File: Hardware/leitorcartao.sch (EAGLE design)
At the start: 157 parts, among them IC1 TL084, IC2 TL084, Q1 DMN3404, Q4 BC847ALT1SMD, Q5 BC847ALT1SMD, Q6 BC847ALT1SMD, Q7 BC847ALT1SMD, Q8 MMBT4403, Q9 MMBT4401, U1 SAMD20E14A-AUT, U3 TLV1117-50CDCYR, U4 MFRC52202HN1, U5 LP2985-33DBVR, X1 ANTENA 125kHz, X2 MIFARE ANTENA

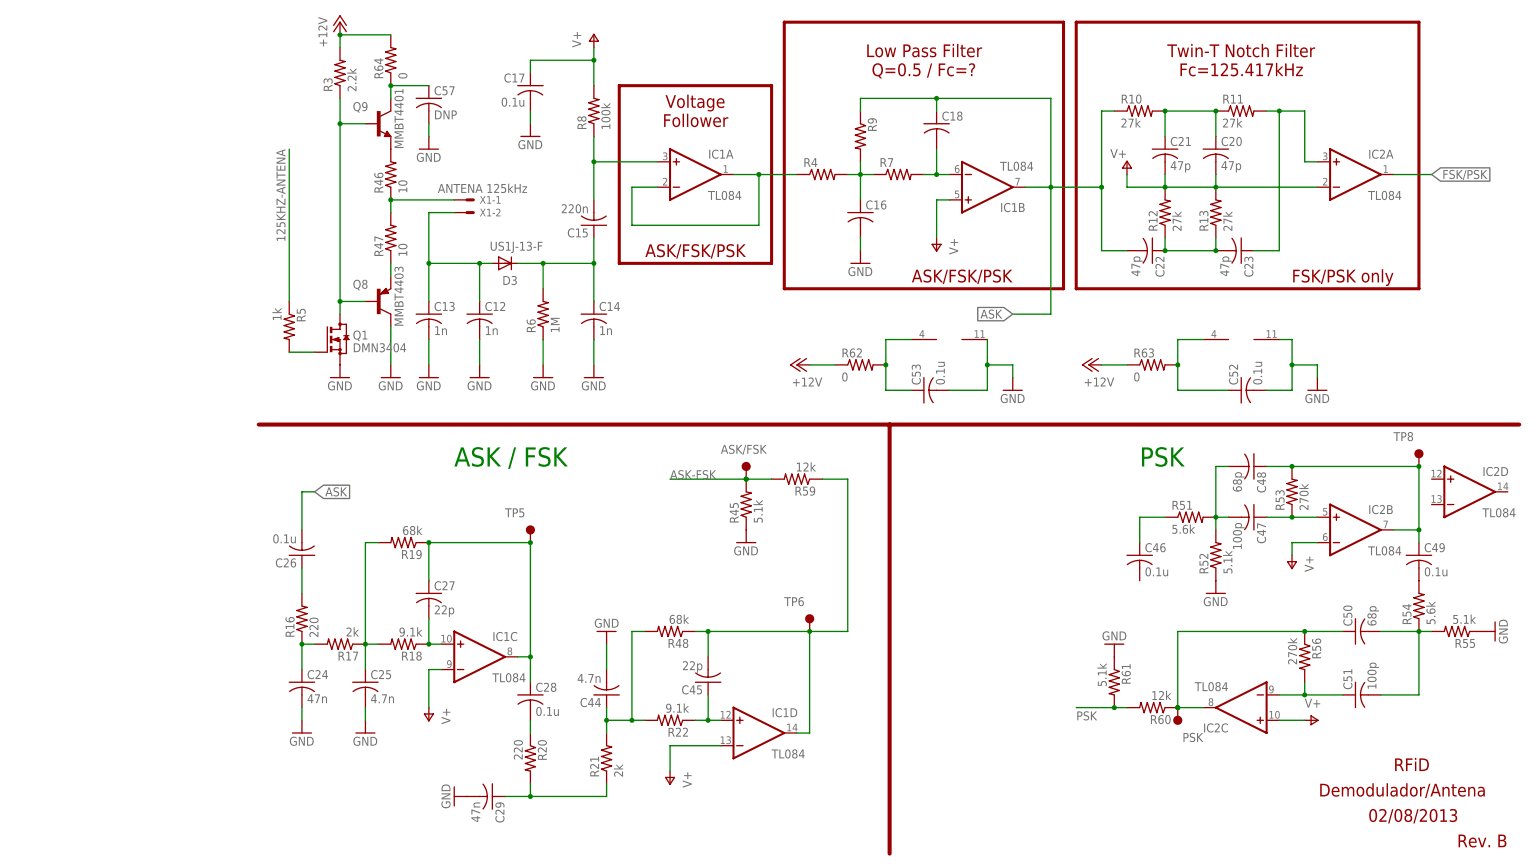
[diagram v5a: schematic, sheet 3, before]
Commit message: Novas alterações do esquema do RFID. ASK com valores já calculados.
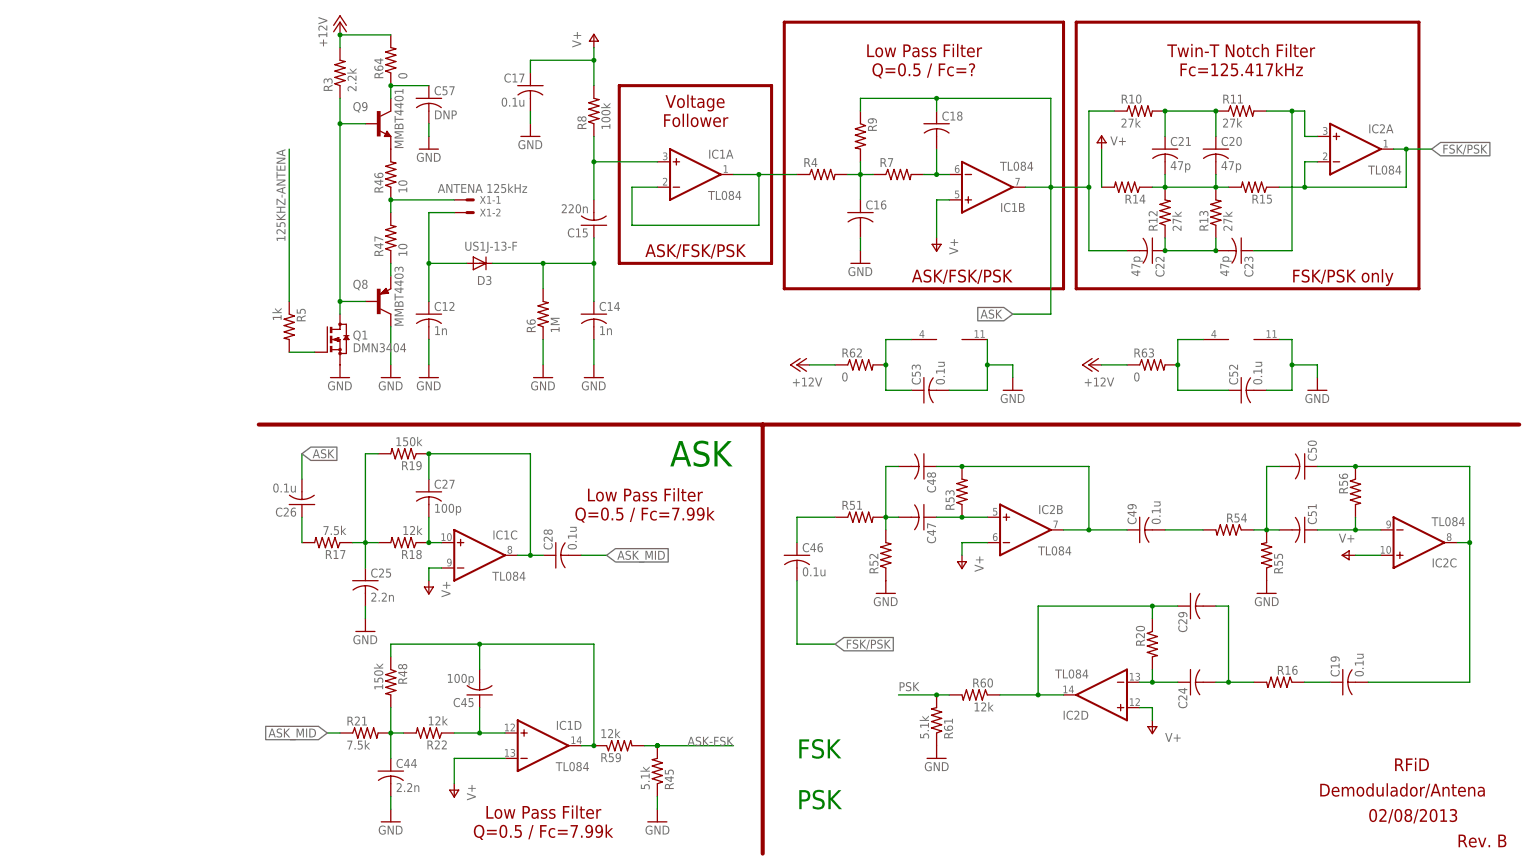
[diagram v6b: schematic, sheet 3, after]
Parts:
- removed ASK/FSK, PSK, TP5, TP6, TP8: TESTPOINT, RFiD:TESTPOINT
- removed C13: 1n, RFiD:C-USC1206
- added C19: 0.1u, RFiD:C-USC0402
- added R14, R15: (no value), RFiD:R-US_R0402
- C24, C29: value 47n -> (none)
- C25, C44: value 4.7n -> 2.2n
- C27, C45: value 22p -> 100p
- C47, C51: value 100p -> (none)
- C48, C50: value 68p -> (none)
- R16, R20: value 220 -> (none)
- R17, R21: value 2k -> 7.5k
- R18, R22: value 9.1k -> 12k
- R19, R48: value 68k -> 150k
- R51, R54: value 5.6k -> (none)
- R52, R55: value 5.1k -> (none)
- R53, R56: value 270k -> (none)
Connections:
- removed net N$22 (its old number): C26.1, R16.2
- removed net N$28: C27.1, C28.1, IC1C.OUT, R19.1, TP5.1
- new net ASK_MID: C28.2, R21.1
- new net N$17: C20.2, C21.2, R12.2, R13.2, R14.1, R15.2
- new net N$21: C26.1, R17.2
- new net N$26: C24.1, IC2D.-IN, R20.2
- new net N$56: C27.1, C28.1, IC1C.OUT, R19.1
- net ASK-FSK: no longer ASK/FSK.1
- net FSK/PSK: now also C46.2, IC2A.-IN, R15.1
- net GND: no longer C13.2, C24.2, C29.2
- net N$24: now also C29.1, IC2D.OUT, R20.1, R60.1; no longer C24.1, R16.1, R17.2
- net N$29: now also C24.2, C29.2, R16.2; no longer C28.2, R20.1
- net N$30: now also C19.1, R16.1; no longer C29.1, R20.2, R21.1
- net N$40: now also C19.2; no longer PSK.1, R60.1
- net N$71: no longer TP8.1
- net N$9: no longer C13.1
- net N$90: no longer TP6.1
- net V+: now also IC2D.+IN, R14.2; no longer C20.2, C21.2, IC2A.-IN, R12.2, R13.2
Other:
- note added: "ASK"
- note added: "FSK"
- note added: "Low Pass Filter Q=0.5 / Fc=7.99k"
- note removed: "ASK / FSK"
- moved on the sheet: C12, C24, C25, C26, C27, C28, C29, C44, C45, C46, C47, C48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

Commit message: Finalização do esquema do RFID, falta valores de PSK e FSK.
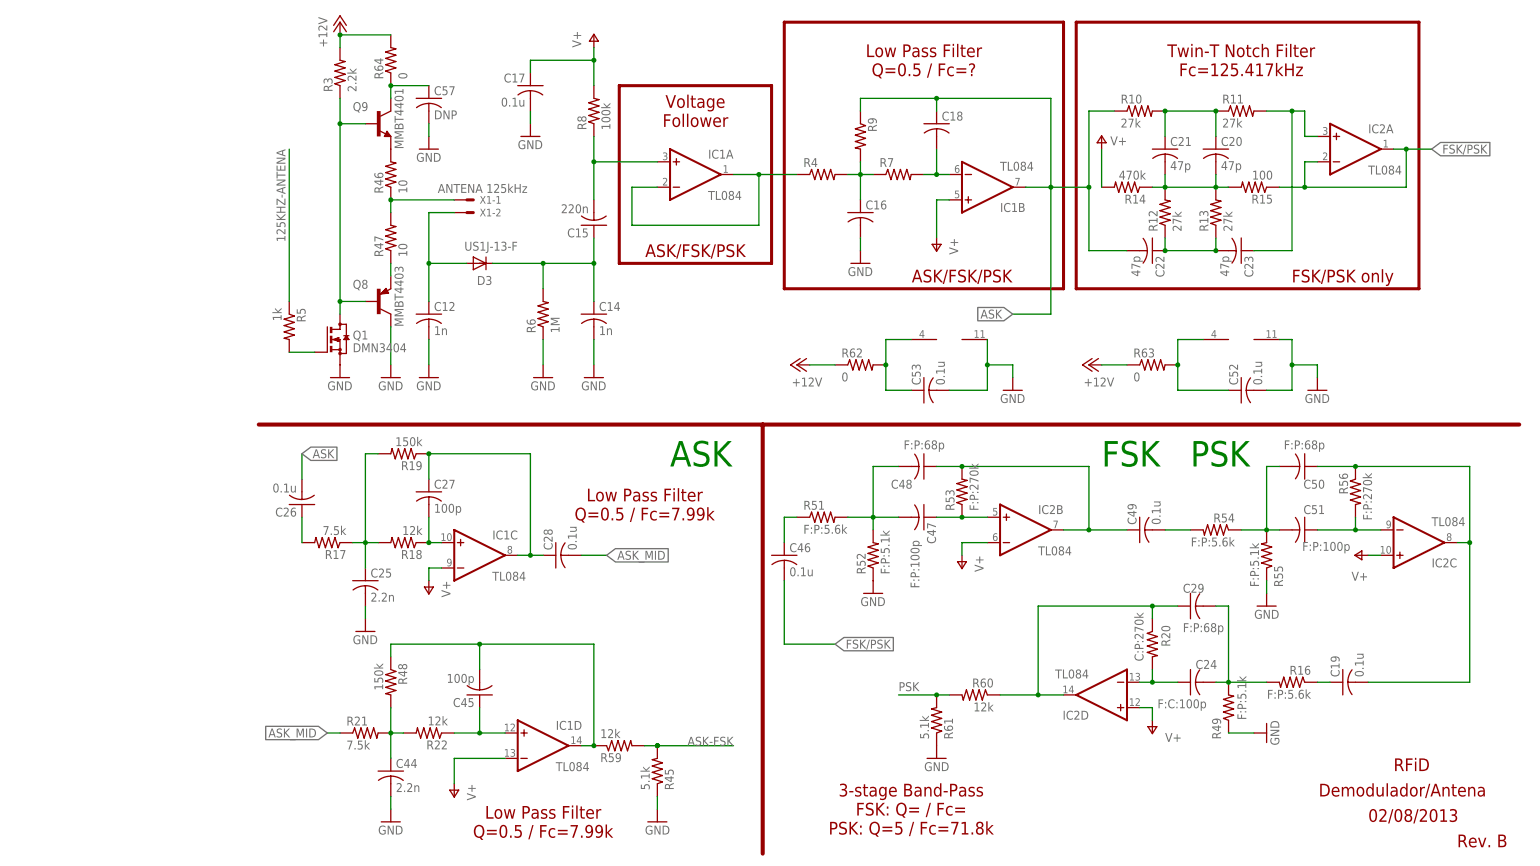
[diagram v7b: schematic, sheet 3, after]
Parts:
- added R49: F:P:5.1k, RFiD:R-US_R0402
- C24: value (none) -> F:C:100p
- C29, C48, C50: value (none) -> F:P:68p
- C47, C51: value (none) -> F:P:100p
- R14: value (none) -> 470k
- R15: value (none) -> 100
- R16, R51, R54: value (none) -> F:P:5.6k
- R20: value (none) -> C:P:270k
- R52, R55: value (none) -> F:P:5.1k
- R53, R56: value (none) -> F:P:270k
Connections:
- net GND: now also R49.1
- net N$29: now also R49.2
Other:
- note added: "3-stage Band-Pass FSK: Q= / Fc= PSK: Q=5 / Fc=71.8k"
- moved on the sheet: C46, R16, R51, R52, R54

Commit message: Correção de conexões dos OpAmps.
Alteração de valores do ASK.
Correções na topologia do PSK.
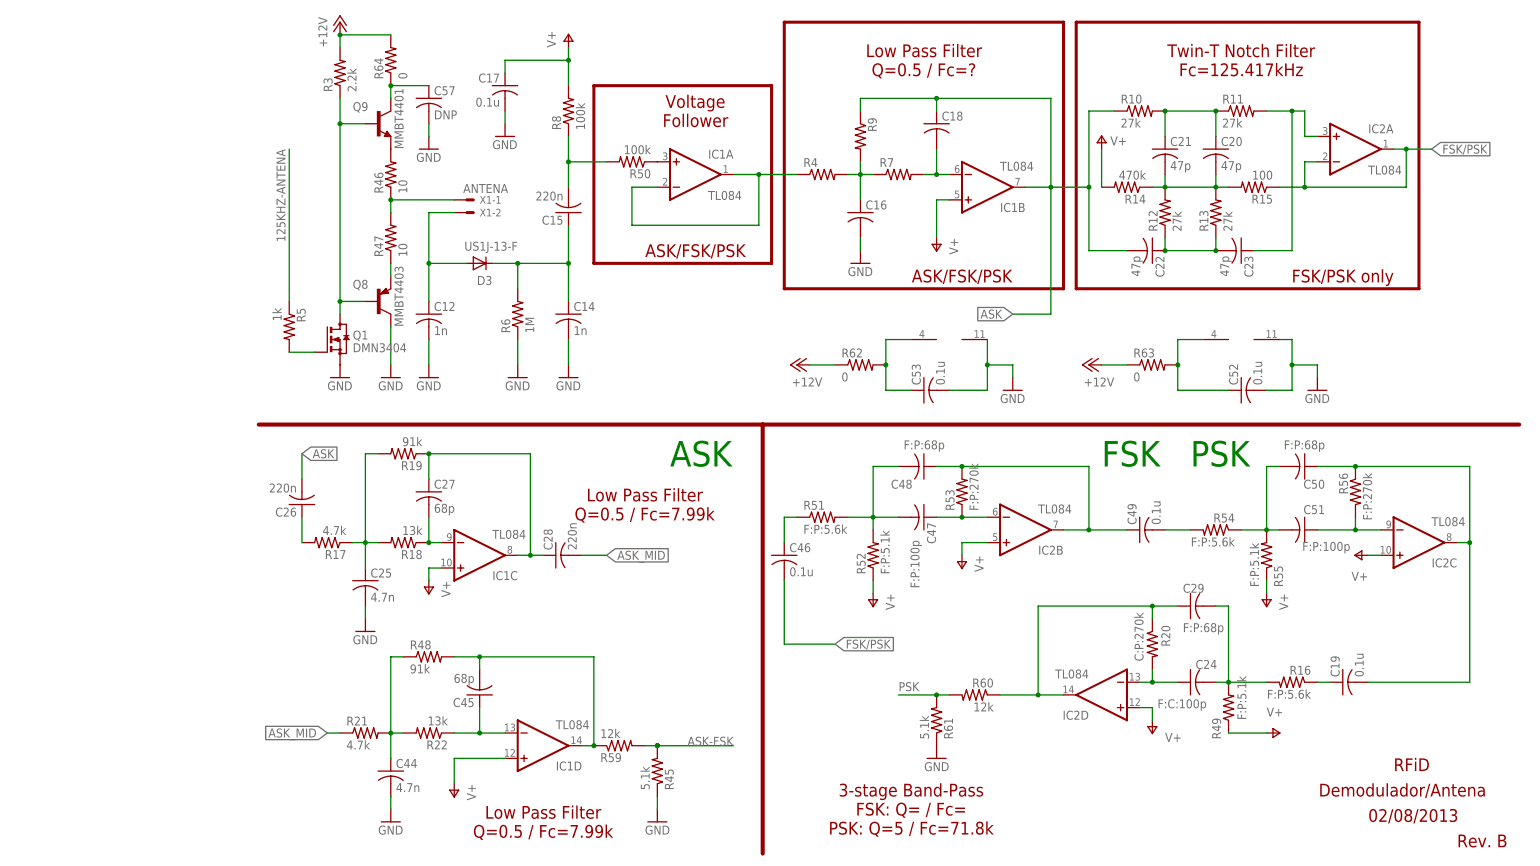
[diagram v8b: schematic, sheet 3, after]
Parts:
- added R50: 100k, RFiD:R-US_R0402
- C25, C44: value 2.2n -> 4.7n
- C26, C28: value 0.1u -> 220n
- C27, C45: value 100p -> 68p
- R17, R21: value 7.5k -> 4.7k
- R18, R22: value 12k -> 13k
- R19, R48: value 150k -> 91k
- X1: value ANTENA 125kHz -> ANTENA
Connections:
- new net N$58: IC1A.+IN, R50.1
- net GND: no longer R49.1, R52.1, R55.1
- net N$14: now also R50.2; no longer IC1A.+IN
- net N$27: now also IC1C.-IN; no longer IC1C.+IN
- net N$63: now also R48.1; no longer R48.2
- net N$64: now also IC1D.-IN; no longer IC1D.+IN
- net N$72: now also IC2B.-IN; no longer IC2B.+IN
- net N$90: now also R48.2; no longer R48.1
- net V+: now also IC1C.+IN, IC1D.+IN, IC2B.+IN, R49.1, R52.1, R55.1; no longer IC1C.-IN, IC1D.-IN, IC2B.-IN
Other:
- moved on the sheet: C14, C15, C17, IC1C, IC1D, IC2B, R48, R6, R8
